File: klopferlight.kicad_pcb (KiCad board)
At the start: 2 copper layers, 172 x 138 mm, 112 parts, among them J10 Output, J2 AMASS_XT60-M_1x02_P7.20mm_Ver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, J3 AMASS_XT60-F_1x02_P7.20mm_Ver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, J7 Conn_01x03_Pin, J8 Conn_01x03_Pin, J9 Input

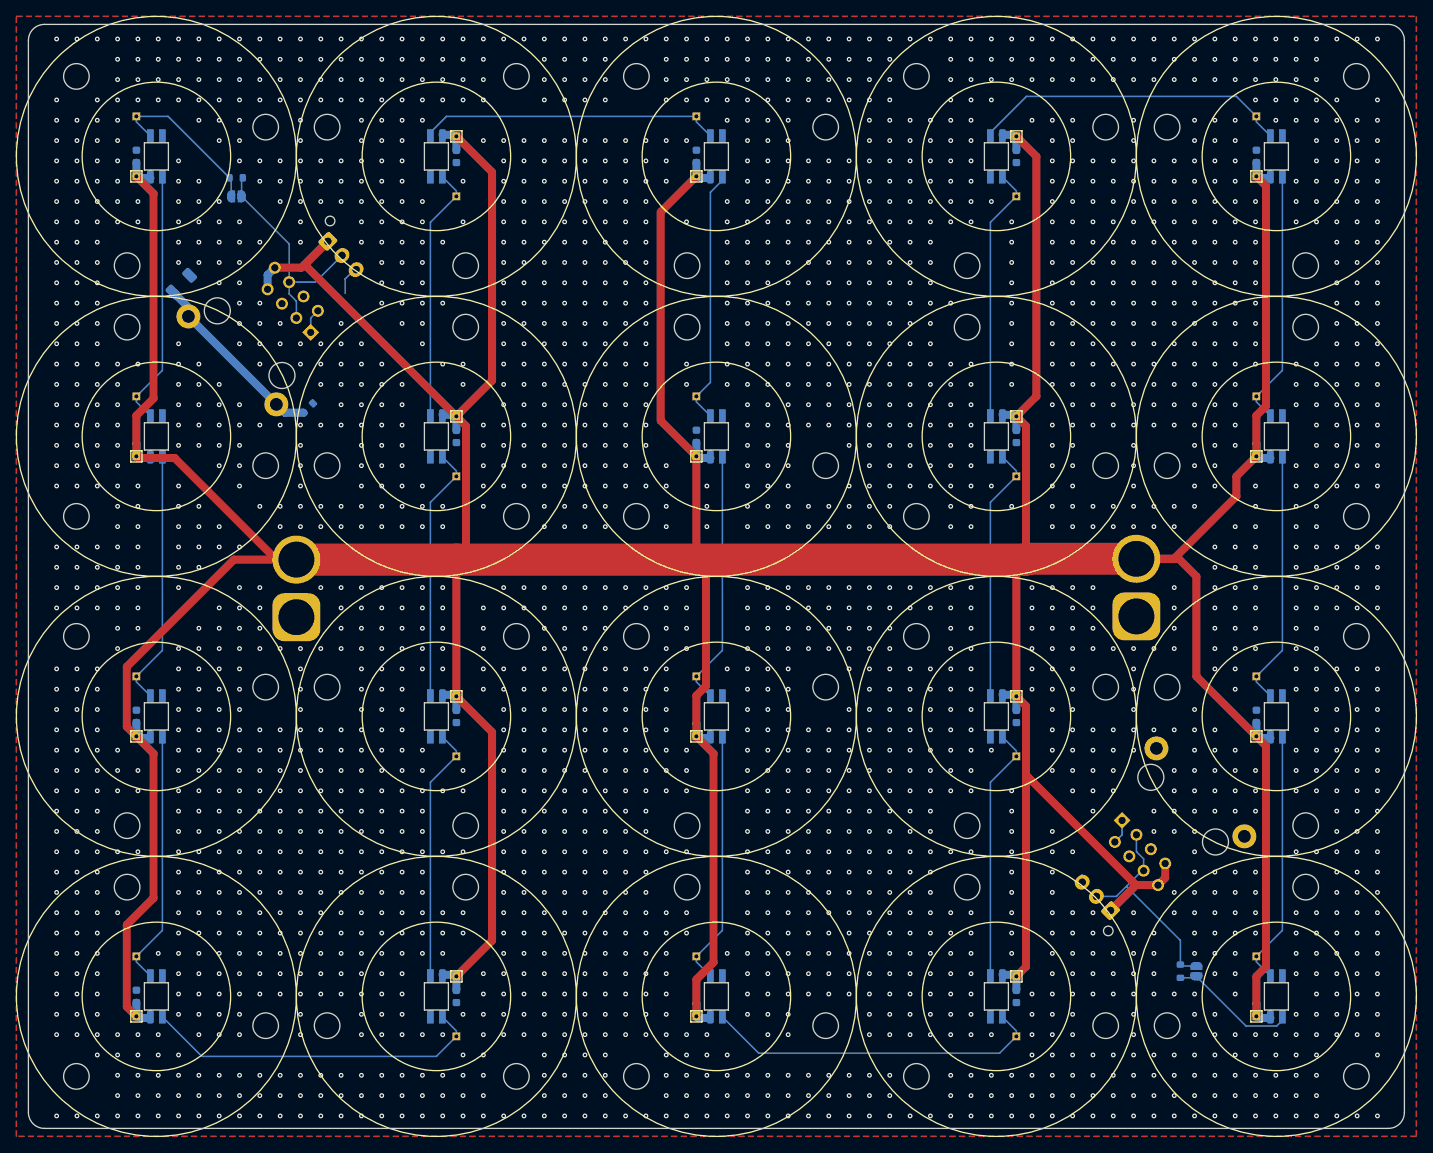
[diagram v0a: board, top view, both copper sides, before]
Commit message: changed pcb outline
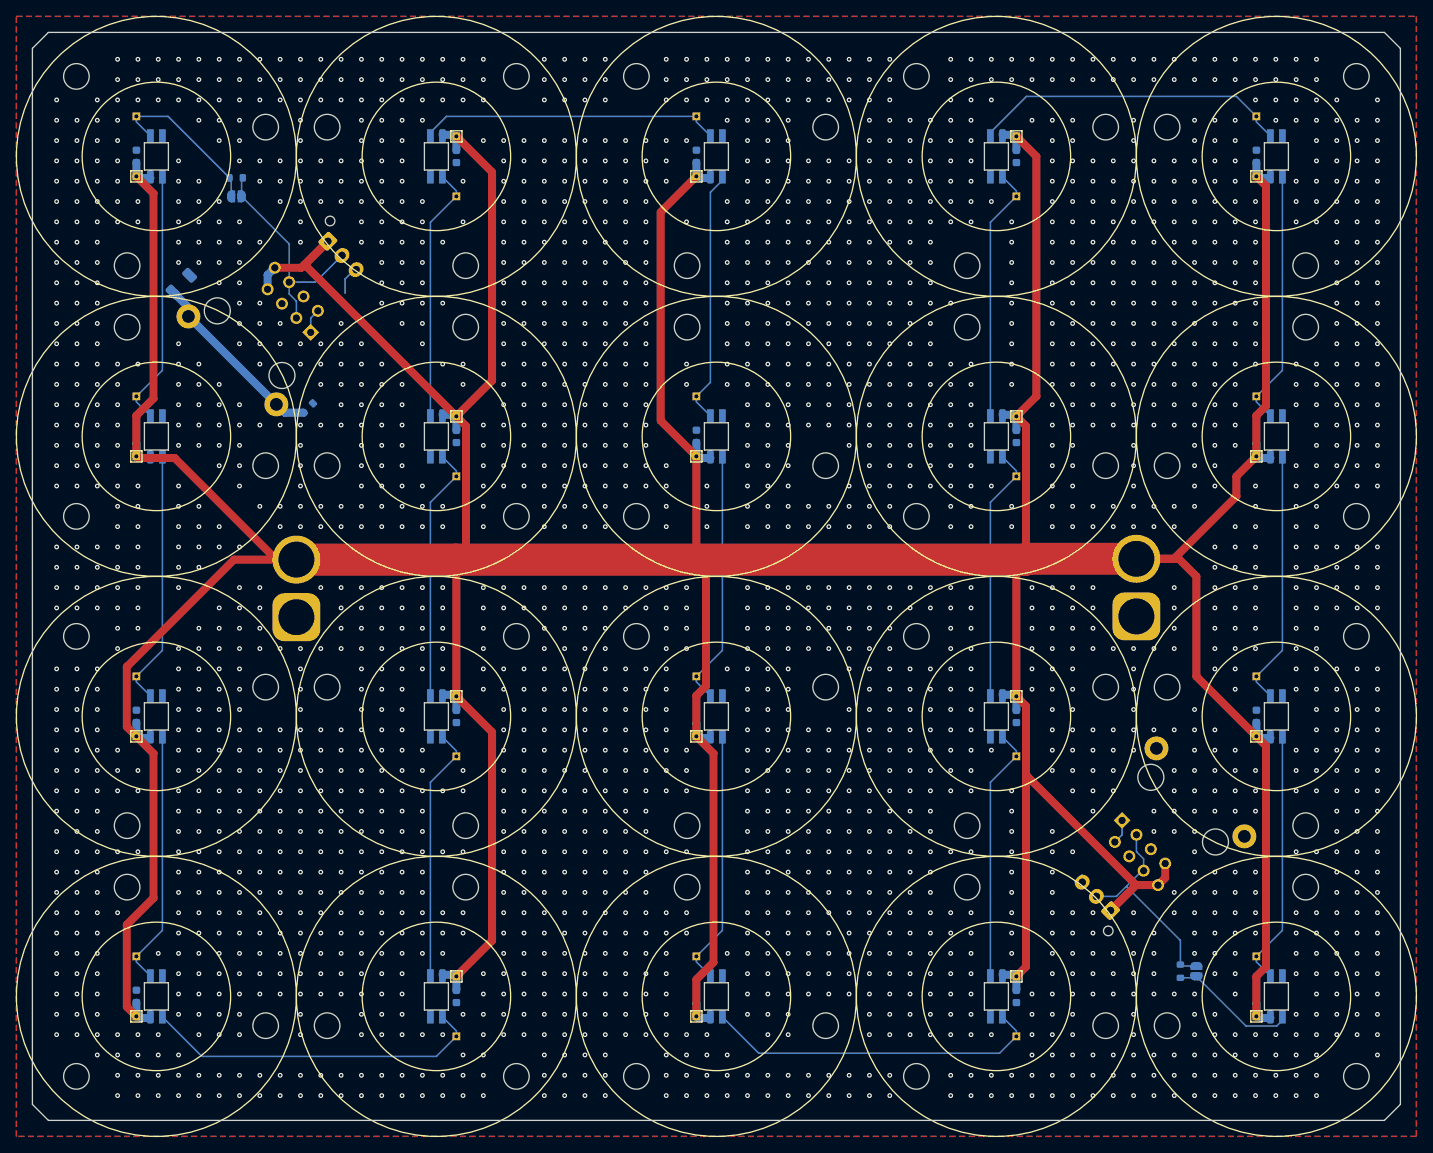
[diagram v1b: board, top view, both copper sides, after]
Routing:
- net GND: vias 2523 -> 2394
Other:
- board size 172 x 138 mm -> 171 x 136 mm
- board text removed: "8x4 Matelightlookalike would be 1408x568 (with 176x142 crates)."

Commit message: snap
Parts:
- removed J10: Output, Connector_RJ:RJ45_Ninigi_GE
- removed J9: Input, Connector_RJ:RJ45_Ninigi_GE
- added C22: 330uF 25V, Capacitor_SMD:CP_Elec_8x10.5, B.Cu at (90.5, 90.5)
- added F1: 16V 1.5A, Fuse:Fuse_1206_3216Metric, B.Cu at (97.5, 85.0)
- added J14: Input, Connector_RJ:RJ45_RCH_RC01937, B.Cu at (106.8, 59.5)
- added J15: Output, Connector_RJ:RJ45_RCH_RC01937, B.Cu at (208.2, 120.5)
- TP21, TP22, TP23, TP24, TP25, TP26, TP27, TP29, TP30, TP31, TP32, TP33, TP34, TP35, TP36, TP37, TP38, TP39, TP40: moved to B.Cu
- moved C20 0.71 mm to (225.5, 142.0)
- moved D20 0.71 mm to (228.0, 142.0)
- moved TP20 0.71 mm to (225.5, 137.0)
- moved TP22 0.71 mm to (125.5, 104.5), turned to 180 degrees
- turned TP21 to 180 degrees
- turned TP23 to 180 degrees
- turned TP24 to 180 degrees
- turned TP25 to 180 degrees
- turned TP26 to 180 degrees
- turned TP27 to 180 degrees
- turned TP29 to 180 degrees
- turned TP30 to 180 degrees
- turned TP31 to 180 degrees
- turned TP32 to 180 degrees
- turned TP33 to 180 degrees
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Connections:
- J2 pad 2: VDD -> Vin
- J3 pad 2: VDD -> Vin
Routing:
- net Vin: track 0.00 -> 112.3 mm
- net VDD: track 840.2 -> 820.3 mm, vias 0 -> 2
- net GND: track 4.34 -> 0.00 mm, vias 2394 -> 2434
- net Net-(J15-Pad1): track 0.00 -> 3.07 mm
- net Net-(J14-Pad1): track 0.00 -> 3.07 mm
- net Net-(J9-Pad1): track 3.07 -> 0.00 mm
- net Net-(J10-Pad1): track 3.07 -> 0.00 mm
- net /Klopfer Module7/D_{out}: track 37.7 -> 39.5 mm, vias 0 -> 1
- net D_{out}: track 26.7 -> 27.8 mm
- net /Klopfer Module11/D_{out}: track 42.7 -> 43.6 mm, vias 0 -> 1
- net D_{in}: track 28.4 -> 29.3 mm
- net /Klopfer Module19/D_{out}: track 16.1 -> 16.9 mm
- net /Klopfer Module10/D_{out}: track 32.0 -> 32.7 mm
- net /Klopfer Module4/D_{out}: track 32.0 -> 32.7 mm
- net /Klopfer Module2/D_{out}: track 32.0 -> 32.7 mm
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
